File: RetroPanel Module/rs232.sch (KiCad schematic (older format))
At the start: 7 parts, among them J11 RS-232, U1 MAX232

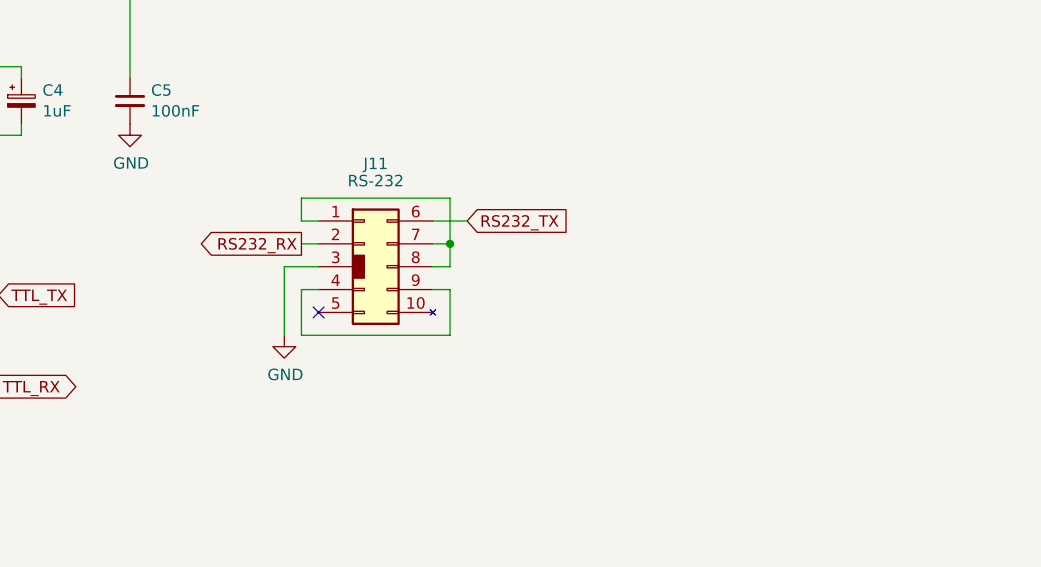
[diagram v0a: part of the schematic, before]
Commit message: Fixed RS-232 connector and export files for second prototype
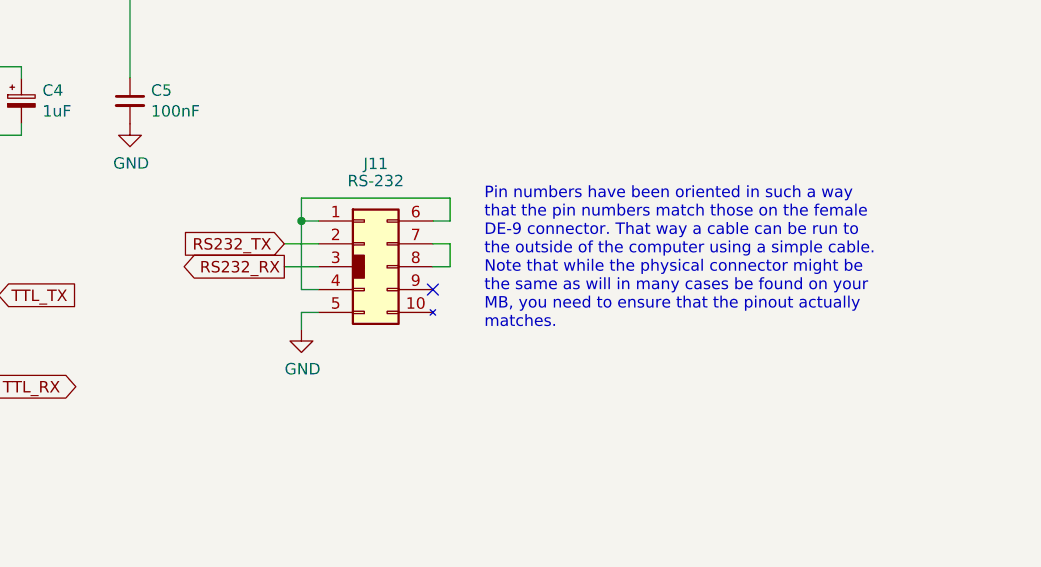
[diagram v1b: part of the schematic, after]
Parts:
- J11: footprint Connector_IDC:IDC-Header_2x05_P2.54mm_Vertical -> RetroPanel:IDC-RS-232-Female
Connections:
- net GND: now also J11.5 (Pin_5); no longer J11.3 (Pin_3)
- net RS232_RX: now also J11.3 (Pin_3); no longer J11.2 (Pin_2)
- net RS232_TX: now also J11.2 (Pin_2); no longer J11.6 (Pin_6)
- net at J11.7 (Pin_7), J11.8 (Pin_8): no longer J11.1 (Pin_1)
- net at J11.4 (Pin_4): now also J11.1 (Pin_1), J11.6 (Pin_6); no longer J11.9 (Pin_9)
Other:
- note added: "Pin numbers have been oriented in such a way\nthat the pin numbers match those on the female\nDE-9 connector. That way a cable can be run to\nthe outside of the computer using a simple cable.\nNote that while the physical connector might be\nthe same as will in many cases be found on your\nMB, you need to ensure that the pinout actually\nmatches."
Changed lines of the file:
@@
 F 0 "J11" H 7975 4450 50  0000 C CNN
 F 1 "RS-232" H 7975 4375 50  0000 C CNN
-F 2 "Connector_IDC:IDC-Header_2x05_P2.54mm_Vertical" H 7925 4000 50  0001 C CNN
+F 2 "RetroPanel:IDC-RS-232-Female" H 7925 4000 50  0001 C CNN
 F 3 "~" H 7925 4000 50  0001 C CNN
 	1    7925 4000
@@
 L power:GND #PWR0117
 U 1 1 635FEC33
-P 7575 4300
-F 0 "#PWR0117" H 7575 4050 50  0001 C CNN
-F 1 "GND" H 7580 4127 50  0000 C CNN
-F 2 "" H 7575 4300 50  0001 C CNN
-F 3 "" H 7575 4300 50  0001 C CNN
-	1    7575 4300
+P 7650 4275
+F 0 "#PWR0117" H 7650 4025 50  0001 C CNN
+F 1 "GND" H 7655 4102 50  0000 C CNN
+F 2 "" H 7650 4275 50  0001 C CNN
+F 3 "" H 7650 4275 50  0001 C CNN
+	1    7650 4275
 	1    0    0    -1
 $EndComp
-Wire Wire Line
-	7575 4300 7575 4000
-NoConn ~ 7725 4200
-Wire Wire Line
-	7725 3800 7650 3800
-Wire Wire Line
-	7650 3800 7650 3700
-Wire Wire Line
-	7650 3700 8300 3700
-Wire Wire Line
-	8300 3700 8300 3900
-Wire Wire Line
-	8300 3900 8225 3900
-Wire Wire Line
-	8300 3900 8300 4000
-Wire Wire Line
-	8300 4000 8225 4000
-Connection ~ 8300 3900
-Text GLabel 7650 3900 0    50   Output ~ 0
+Text GLabel 7575 4000 0    50   Output ~ 0
 RS232_RX
-Wire Wire Line
-	7650 3900 7725 3900
-Wire Wire Line
-	7575 4000 7725 4000
-Wire Wire Line
-	7725 4100 7650 4100
-Wire Wire Line
-	7650 4100 7650 4300
-Wire Wire Line
-	7650 4300 8300 4300
-Wire Wire Line
-	8300 4300 8300 4100
-Wire Wire Line
-	8300 4100 8225 4100
-Text GLabel 8375 3800 2    50   Input ~ 0
+Text GLabel 7575 3900 0    50   Input ~ 0
 RS232_TX
 Wire Wire Line
-	8375 3800 8225 3800
+	7575 3900 7725 3900
 $Comp
 L Device:CP_Small C3
@@
 Text Notes 4475 5850 0    50   ~ 0
 C1-C4 may be 100nF monolithic capacitors when\nused with MAX232A IC. When used with the common\ncheaper alternatives such as MAX232CPE, these need\nto be 1uF polarized electrolytic capacitors.
+Wire Wire Line
+	7725 3800 7650 3800
+Wire Wire Line
+	7650 3800 7650 4100
+Wire Wire Line
+	7650 4100 7725 4100
+Wire Wire Line
+	7650 3800 7650 3700
+Wire Wire Line
+	7650 3700 8300 3700
+Wire Wire Line
+	8300 3700 8300 3800
+Wire Wire Line
+	8300 3800 8225 3800
+Connection ~ 7650 3800
+Wire Wire Line
+	7575 4000 7725 4000
+Wire Wire Line
+	8225 3900 8300 3900
+Wire Wire Line
+	8300 3900 8300 4000
+Wire Wire Line
+	8300 4000 8225 4000
+NoConn ~ 8225 4100
+Wire Wire Line
+	7650 4275 7650 4200
+Wire Wire Line
+	7650 4200 7725 4200
+Text Notes 8450 4275 0    50   ~ 0
+Pin numbers have been oriented in such a way\nthat the pin numbers match those on the female\nDE-9 connector. That way a cable can be run to\nthe outside of the computer using a simple cable.\nNote that while the physical connector might be\nthe same as will in many cases be found on your\nMB, you need to ensure that the pinout actually\nmatches.
 $EndSCHEMATC
